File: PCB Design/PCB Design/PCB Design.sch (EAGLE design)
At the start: 6 parts, among them J1 1X2-3.5MM, U1 ADXL337

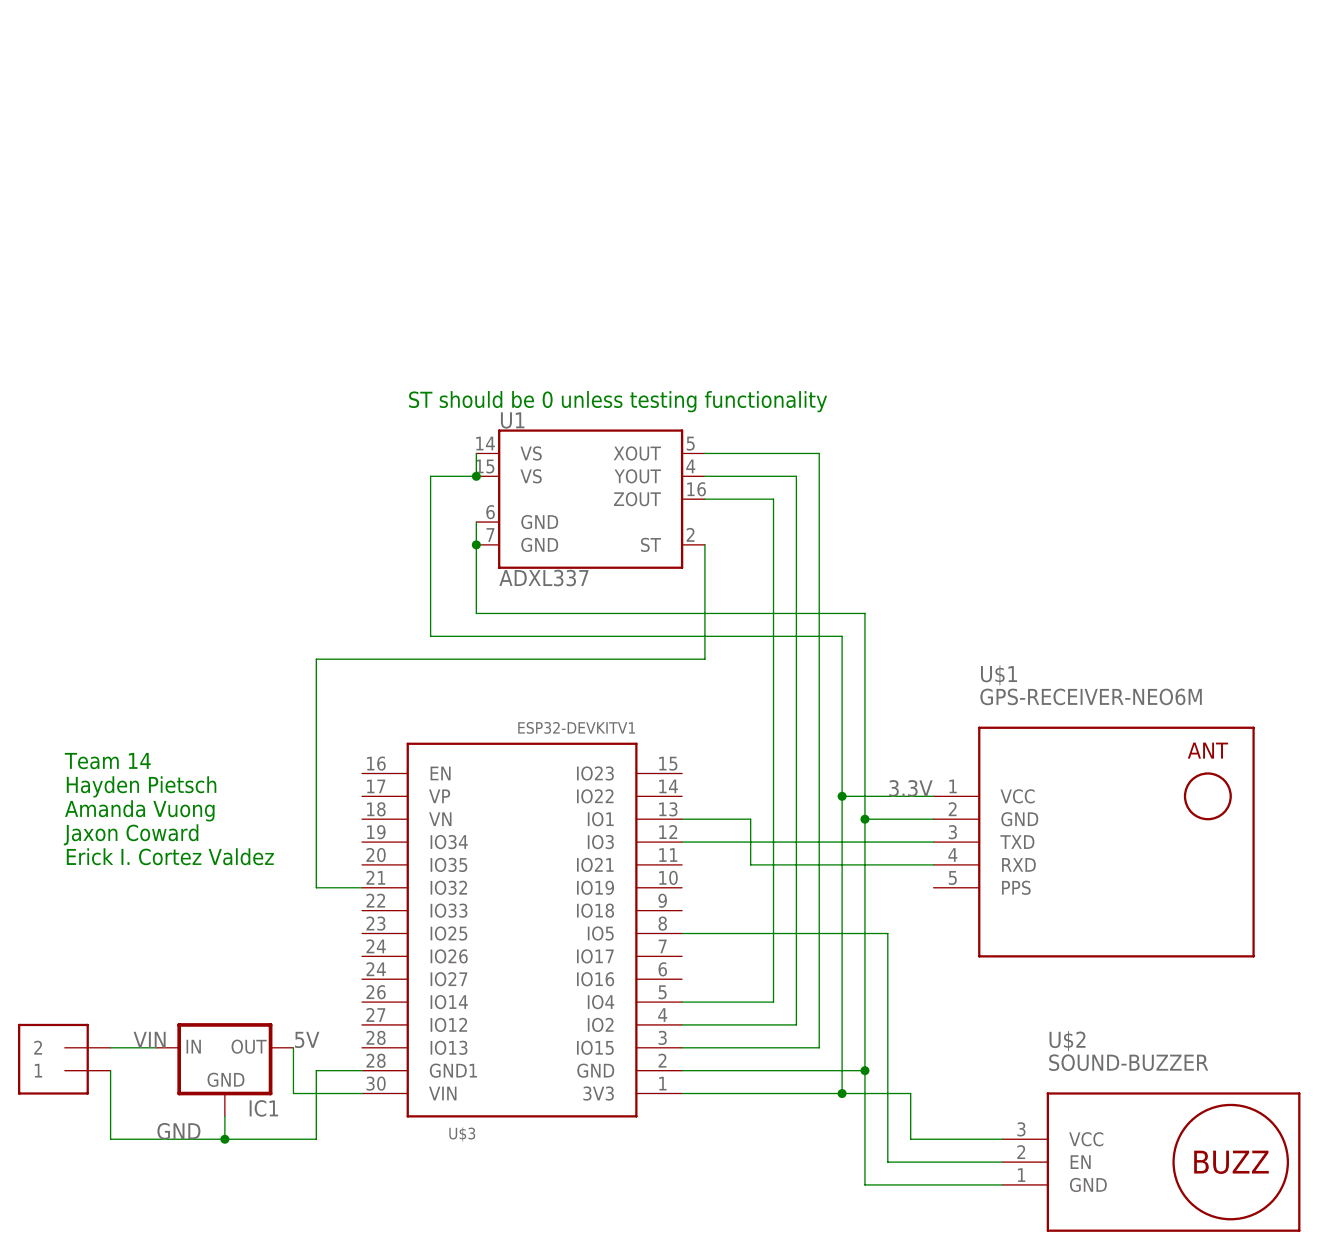
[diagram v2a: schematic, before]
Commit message: Fixed Scematic and Board Based on Shawn's suggestions
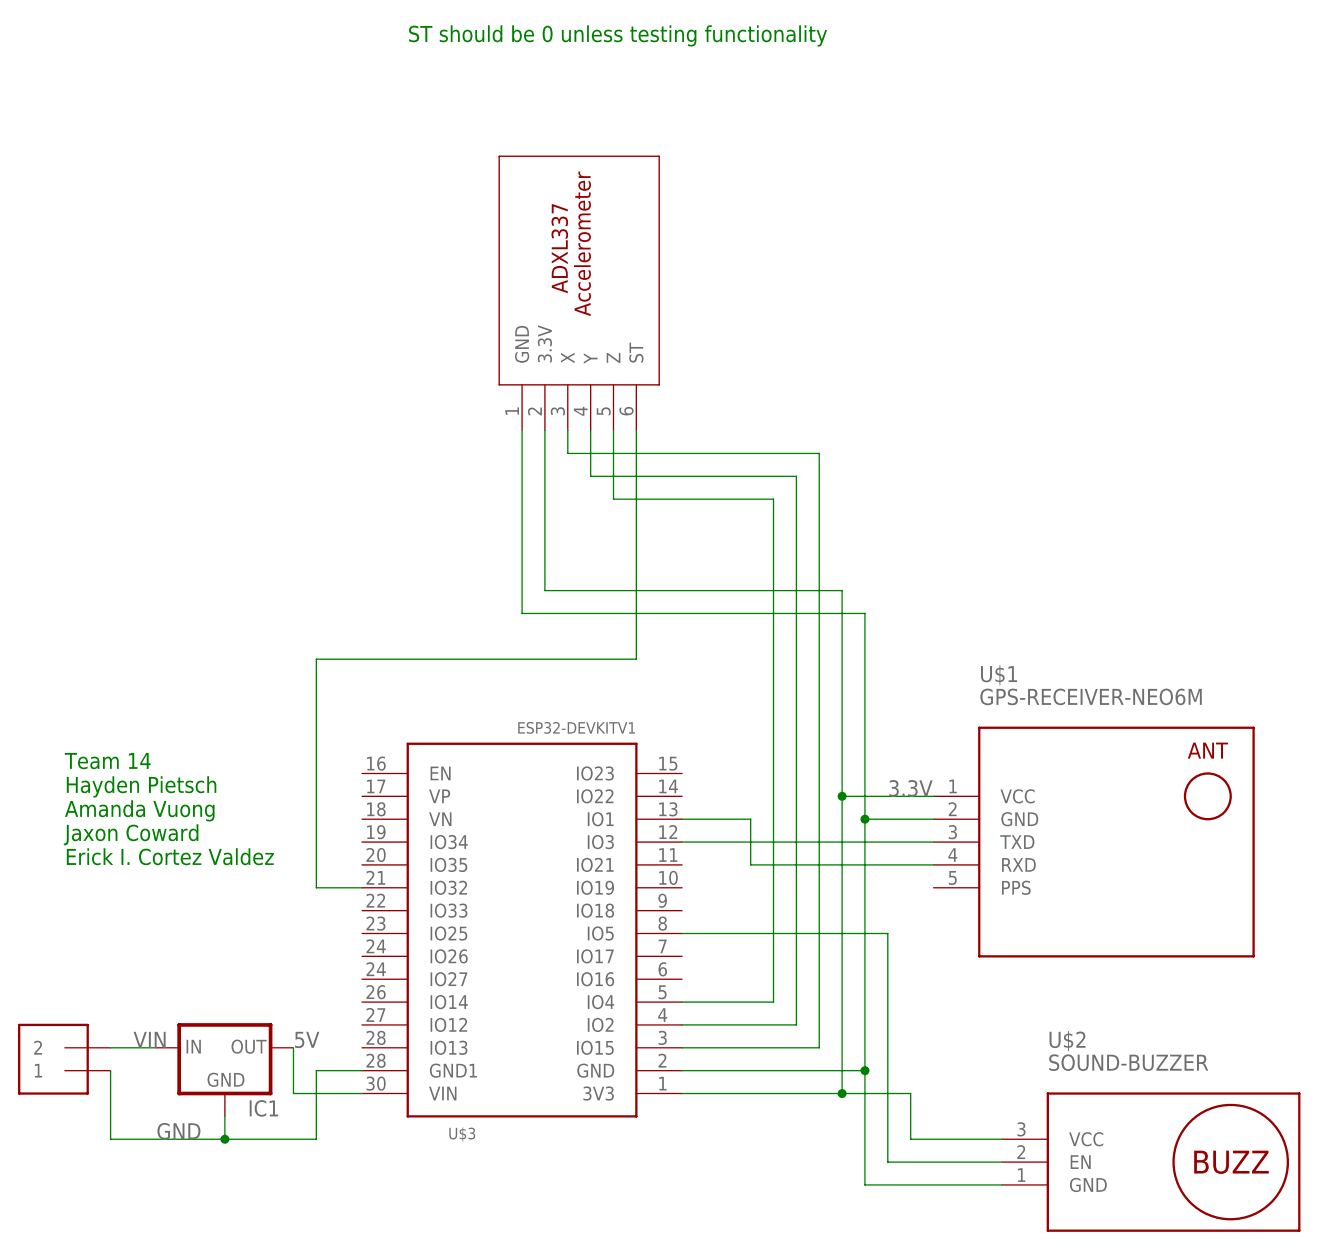
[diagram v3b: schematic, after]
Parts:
- removed U1: ADXL337, SparkFun-Sensors:ADXL337
- added U$4: ADXL337_ACCELEROMETER, ADXL337_Breakout:ADXL337_ACCELEROMETER
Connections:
- net 3.3V: now also U$4.3.3V; no longer U1.VS@1, U1.VS@2
- net GND: now also U$4.GND; no longer U1.GND@1, U1.GND@2
- net N$3: now also U$4.ST; no longer U1.ST
- net N$6: now also U$4.X; no longer U1.XOUT
- net N$7: now also U$4.Y; no longer U1.YOUT
- net N$8: now also U$4.Z; no longer U1.ZOUT
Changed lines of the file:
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@@
-<attribute name="OC_NEWARK" value="unknown"/>
-</part>
-<part name="U1" library="SparkFun-Sensors" deviceset="ADXL337" device="">
-<attribute name="MF" value=""/>
-<attribute name="MPN" value=""/>
 <attribute name="OC_NEWARK" value="unknown"/>
 </part>
@@
 <attribute name="OC_NEWARK" value="34X0689"/>
 </part>
+<part name="U$4" library="ADXL337_Breakout" deviceset="ADXL337_ACCELEROMETER" device=""/>
 </parts>
 <sheets>
 <sheet>
 <plain>
-<text x="-10.16" y="104.14" size="1.778" layer="91">ST should be 0 unless testing functionality</text>
+<text x="-10.16" y="144.78" size="1.778" layer="91">ST should be 0 unless testing functionality</text>
 <text x="-48.26" y="53.34" size="1.778" layer="91">Team 14
 Hayden Pietsch
@@
 <attribute name="MPN" x="73.66" y="20.32" size="1.778" layer="96" display="off"/>
 </instance>
-<instance part="U1" gate="G$1" x="10.16" y="93.98">
-<attribute name="OC_NEWARK" x="10.16" y="93.98" size="1.778" layer="96" display="off"/>
-<attribute name="MF" x="10.16" y="93.98" size="1.778" layer="96" display="off"/>
-<attribute name="MPN" x="10.16" y="93.98" size="1.778" layer="96" display="off"/>
-</instance>
 <instance part="U$3" gate="G$1" x="2.54" y="50.8" rot="R90">
 <attribute name="OC_NEWARK" x="2.54" y="50.8" size="1.778" layer="96" display="off"/>
@@
 <attribute name="MPN" x="-30.48" y="33.02" size="1.778" layer="96" display="off"/>
 </instance>
+<instance part="U$4" gate="G$1" x="17.78" y="106.68" rot="R90"/>
 </instances>
 <busses>
@@
 <wire x1="48.26" y1="60.96" x2="38.1" y2="60.96" width="0.1524" layer="91"/>
 <wire x1="38.1" y1="60.96" x2="38.1" y2="27.94" width="0.1524" layer="91"/>
-<wire x1="38.1" y1="60.96" x2="38.1" y2="78.74" width="0.1524" layer="91"/>
+<wire x1="38.1" y1="60.96" x2="38.1" y2="83.82" width="0.1524" layer="91"/>
 <junction x="38.1" y="60.96"/>
-<wire x1="38.1" y1="78.74" x2="-7.62" y2="78.74" width="0.1524" layer="91"/>
-<pinref part="U1" gate="G$1" pin="VS@2"/>
-<wire x1="-7.62" y1="78.74" x2="-7.62" y2="96.52" width="0.1524" layer="91"/>
-<wire x1="-7.62" y1="96.52" x2="-2.54" y2="96.52" width="0.1524" layer="91"/>
-<pinref part="U1" gate="G$1" pin="VS@1"/>
-<wire x1="-2.54" y1="99.06" x2="-2.54" y2="96.52" width="0.1524" layer="91"/>
-<junction x="-2.54" y="96.52"/>
+<wire x1="38.1" y1="83.82" x2="5.08" y2="83.82" width="0.1524" layer="91"/>
 <wire x1="38.1" y1="27.94" x2="45.72" y2="27.94" width="0.1524" layer="91"/>
 <junction x="38.1" y="27.94"/>
@@
 <wire x1="45.72" y1="22.86" x2="55.88" y2="22.86" width="0.1524" layer="91"/>
 <label x="43.18" y="60.96" size="1.778" layer="95"/>
+<wire x1="5.08" y1="83.82" x2="5.08" y2="101.6" width="0.1524" layer="91"/>
+<pinref part="U$4" gate="G$1" pin="3.3V"/>
 </segment>
 </net>
@@
 <wire x1="20.32" y1="30.48" x2="40.64" y2="30.48" width="0.1524" layer="91"/>
 <junction x="40.64" y="30.48"/>
-<wire x1="40.64" y1="81.28" x2="-2.54" y2="81.28" width="0.1524" layer="91"/>
-<pinref part="U1" gate="G$1" pin="GND@2"/>
-<pinref part="U1" gate="G$1" pin="GND@1"/>
-<wire x1="-2.54" y1="91.44" x2="-2.54" y2="88.9" width="0.1524" layer="91"/>
-<wire x1="-2.54" y1="81.28" x2="-2.54" y2="88.9" width="0.1524" layer="91"/>
-<junction x="-2.54" y="88.9"/>
+<wire x1="40.64" y1="81.28" x2="2.54" y2="81.28" width="0.1524" layer="91"/>
+<wire x1="2.54" y1="81.28" x2="2.54" y2="101.6" width="0.1524" layer="91"/>
+<pinref part="U$4" gate="G$1" pin="GND"/>
 </segment>
 <segment>
@@
 <pinref part="U$3" gate="G$1" pin="IO15"/>
 <wire x1="20.32" y1="33.02" x2="35.56" y2="33.02" width="0.1524" layer="91"/>
-<pinref part="U1" gate="G$1" pin="XOUT"/>
 <wire x1="35.56" y1="33.02" x2="35.56" y2="99.06" width="0.1524" layer="91"/>
-<wire x1="35.56" y1="99.06" x2="22.86" y2="99.06" width="0.1524" layer="91"/>
+<wire x1="35.56" y1="99.06" x2="7.62" y2="99.06" width="0.1524" layer="91"/>
+<wire x1="7.62" y1="99.06" x2="7.62" y2="101.6" width="0.1524" layer="91"/>
+<pinref part="U$4" gate="G$1" pin="X"/>
 </segment>
 </net>
 <net name="N$7" class="0">
 <segment>
-<pinref part="U1" gate="G$1" pin="YOUT"/>
-<wire x1="22.86" y1="96.52" x2="33.02" y2="96.52" width="0.1524" layer="91"/>
 <pinref part="U$3" gate="G$1" pin="IO2"/>
 <wire x1="33.02" y1="96.52" x2="33.02" y2="35.56" width="0.1524" layer="91"/>
 <wire x1="33.02" y1="35.56" x2="20.32" y2="35.56" width="0.1524" layer="91"/>
+<wire x1="33.02" y1="96.52" x2="10.16" y2="96.52" width="0.1524" layer="91"/>
+<wire x1="10.16" y1="96.52" x2="10.16" y2="101.6" width="0.1524" layer="91"/>
+<pinref part="U$4" gate="G$1" pin="Y"/>
 </segment>
 </net>
 <net name="N$8" class="0">
 <segment>
-<pinref part="U1" gate="G$1" pin="ZOUT"/>
-<wire x1="22.86" y1="93.98" x2="30.48" y2="93.98" width="0.1524" layer="91"/>
 <pinref part="U$3" gate="G$1" pin="IO4"/>
 <wire x1="30.48" y1="93.98" x2="30.48" y2="38.1" width="0.1524" layer="91"/>
 <wire x1="30.48" y1="38.1" x2="20.32" y2="38.1" width="0.1524" layer="91"/>
+<wire x1="30.48" y1="93.98" x2="12.7" y2="93.98" width="0.1524" layer="91"/>
+<wire x1="12.7" y1="93.98" x2="12.7" y2="101.6" width="0.1524" layer="91"/>
+<pinref part="U$4" gate="G$1" pin="Z"/>
 </segment>
 </net>
@@
 <wire x1="-15.24" y1="50.8" x2="-20.32" y2="50.8" width="0.1524" layer="91"/>
 <wire x1="-20.32" y1="50.8" x2="-20.32" y2="76.2" width="0.1524" layer="91"/>
-<pinref part="U1" gate="G$1" pin="ST"/>
-<wire x1="-20.32" y1="76.2" x2="22.86" y2="76.2" width="0.1524" layer="91"/>
-<wire x1="22.86" y1="76.2" x2="22.86" y2="88.9" width="0.1524" layer="91"/>
+<wire x1="-20.32" y1="76.2" x2="15.24" y2="76.2" width="0.1524" layer="91"/>
+<wire x1="15.24" y1="76.2" x2="15.24" y2="101.6" width="0.1524" layer="91"/>
+<pinref part="U$4" gate="G$1" pin="ST"/>
 </segment>
 </net>

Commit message: CAD desings
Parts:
- U$4: OC_NEWARK (none) -> unknown
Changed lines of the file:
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@@
 <attribute name="OC_NEWARK" value="34X0689"/>
 </part>
-<part name="U$4" library="ADXL337_Breakout" deviceset="ADXL337_ACCELEROMETER" device=""/>
+<part name="U$4" library="ADXL337_Breakout" deviceset="ADXL337_ACCELEROMETER" device="">
+<attribute name="MF" value=""/>
+<attribute name="MPN" value=""/>
+<attribute name="OC_NEWARK" value="unknown"/>
+</part>
 </parts>
 <sheets>
@@
 <attribute name="MPN" x="-30.48" y="33.02" size="1.778" layer="96" display="off"/>
 </instance>
-<instance part="U$4" gate="G$1" x="17.78" y="106.68" rot="R90"/>
+<instance part="U$4" gate="G$1" x="17.78" y="106.68" rot="R90">
+<attribute name="OC_NEWARK" x="17.78" y="106.68" size="1.778" layer="96" display="off"/>
+<attribute name="MF" x="17.78" y="106.68" size="1.778" layer="96" display="off"/>
+<attribute name="MPN" x="17.78" y="106.68" size="1.778" layer="96" display="off"/>
+</instance>
 </instances>
 <busses>
